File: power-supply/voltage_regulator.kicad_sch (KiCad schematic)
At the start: 22 parts

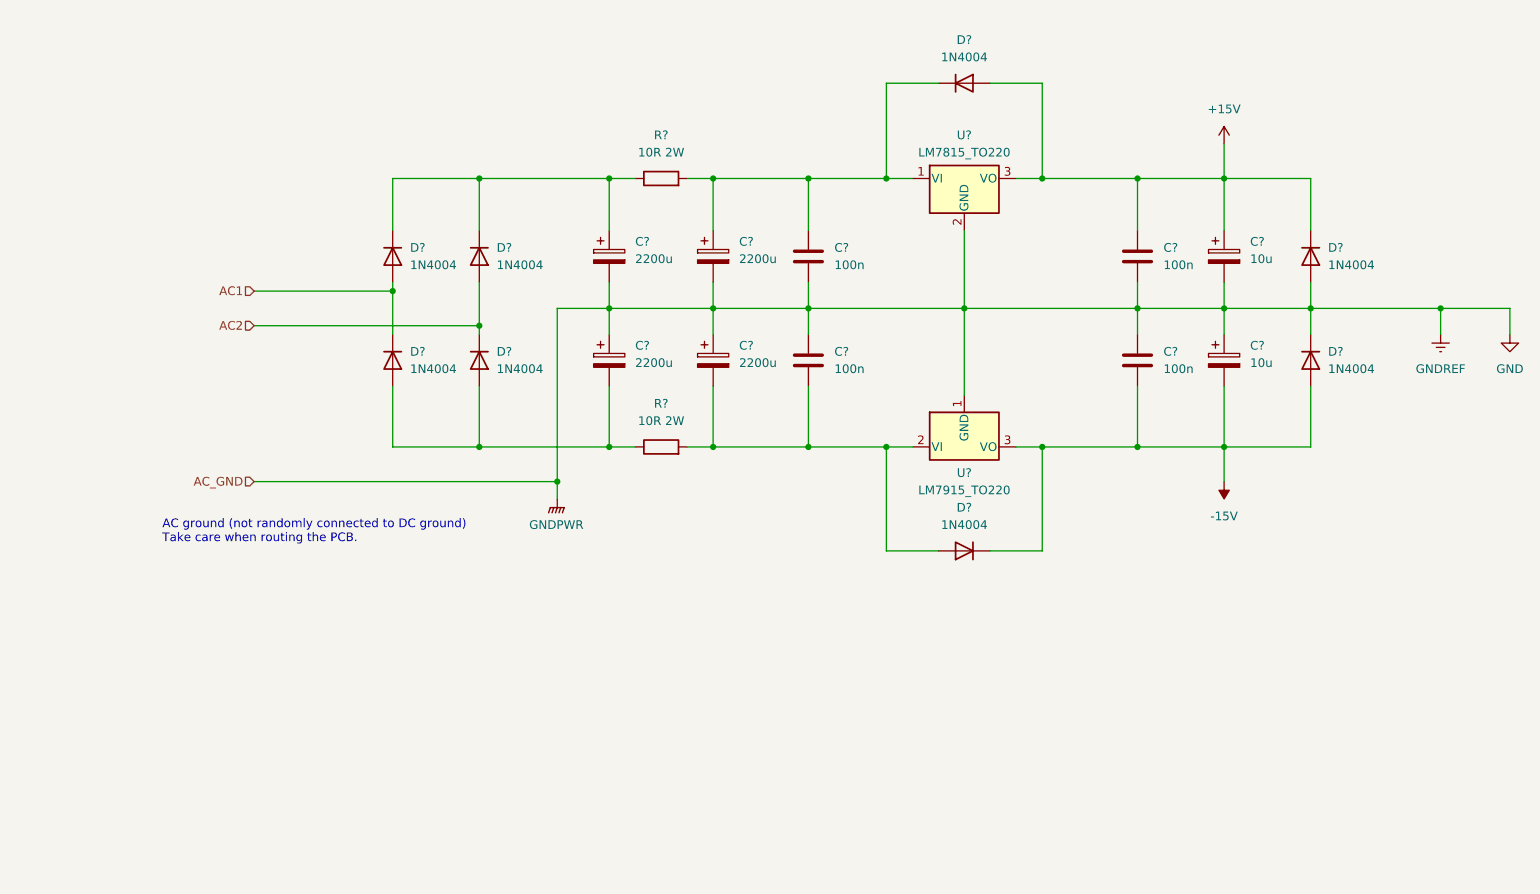
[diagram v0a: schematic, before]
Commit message: Some additions to power supply
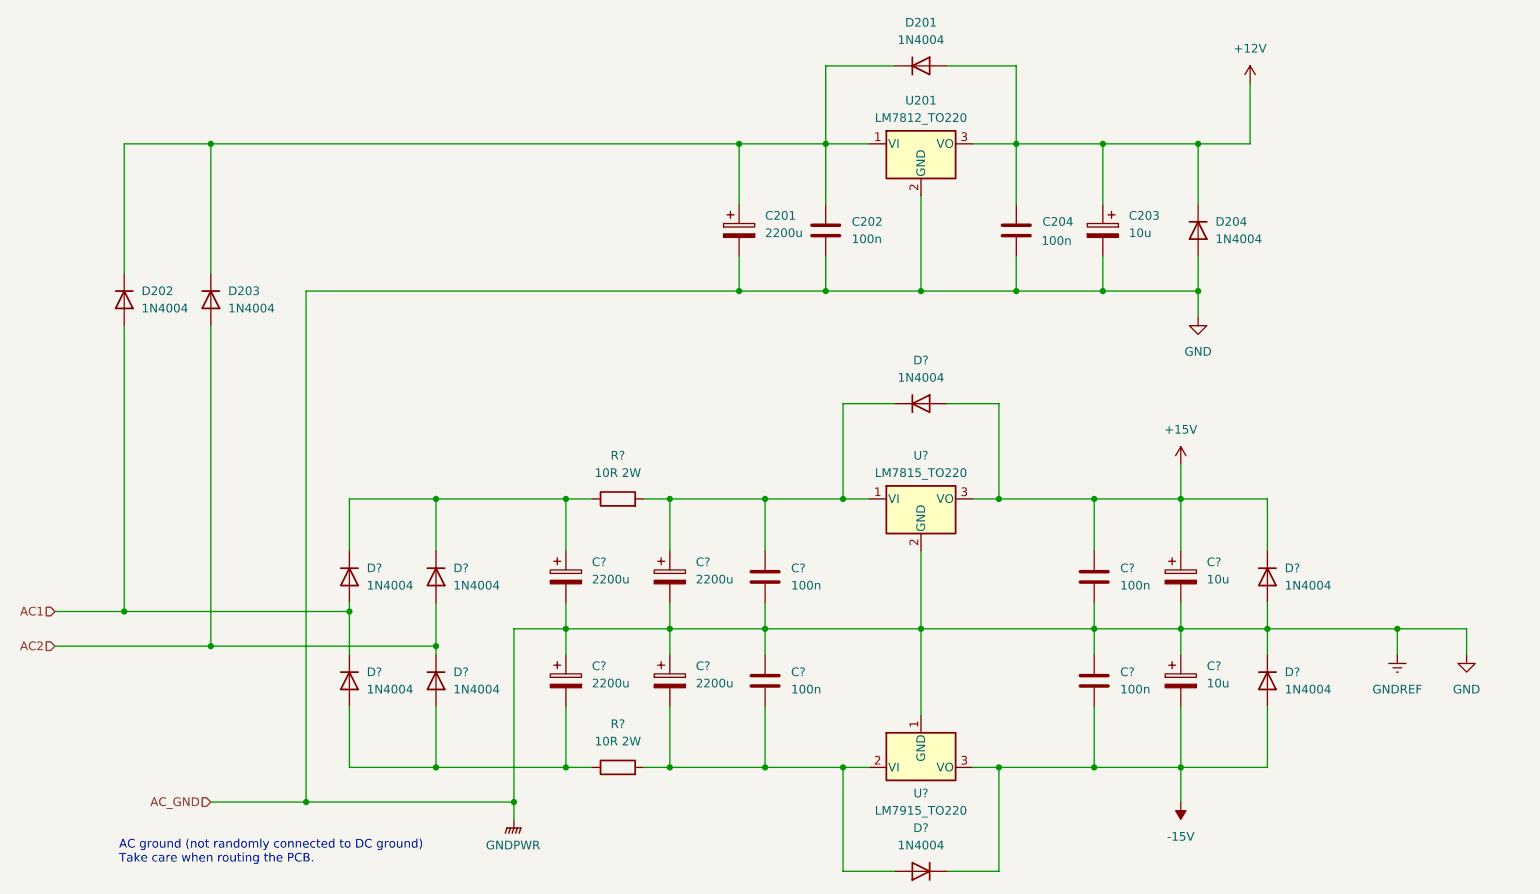
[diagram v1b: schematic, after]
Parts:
- added C201: 2200u, Capacitor_THT:CP_Radial_D18.0mm_P7.50mm, symbol Device:C_Polarized
- added C202, C204: 100n, Capacitor_THT:C_Disc_D6.0mm_W2.5mm_P5.00mm, symbol Device:C
- added C203: 10u, Capacitor_THT:CP_Radial_D5.0mm_P2.00mm, symbol Device:C_Polarized
- added D201, D202, D203, D204: 1N4004, Diode_THT:D_DO-41_SOD81_P10.16mm_Horizontal, symbol Diode:1N4004
- added U201: LM7812_TO220, Package_TO_SOT_THT:TO-220-3_Vertical, symbol Regulator_Linear:LM7812_TO220
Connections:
- net AC1: now also D202.2 (A)
- net AC2: now also D203.2 (A)
- net GND: now also C201.2, C202.2, C203.2, C204.2, D204.2 (A), U201.2 (GND)
- new net: C201.1, C202.1, D201.1 (K), D202.1 (K), D203.1 (K), U201.1 (VI)
- new net +12V: C203.1, C204.1, D201.2 (A), D204.1 (K), U201.3 (VO)
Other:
- moved on the sheet: C?, D?, R?, U?
